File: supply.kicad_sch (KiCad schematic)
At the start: 151 parts, among them IC1 TPS54561, J3 DC_SOCKET, J8 61300311121, U10 LM3881MME_NOPB, U12 AP62301WU-7, U17 SN74LVC1G125DBVR, U18 MAX812REUS+T, U19 PAC1954T-E/4MX, U2 TPS65295RJET, U20 PAC1954T-E/4MX, U21 SN74LVC1G125DBVR, U22 SN74LVC1G125DBVR, U23 SN74LVC1G125DBVR, U4 AP62301WU-7, U5 AP62301WU-7, U9 AP62301WU-7

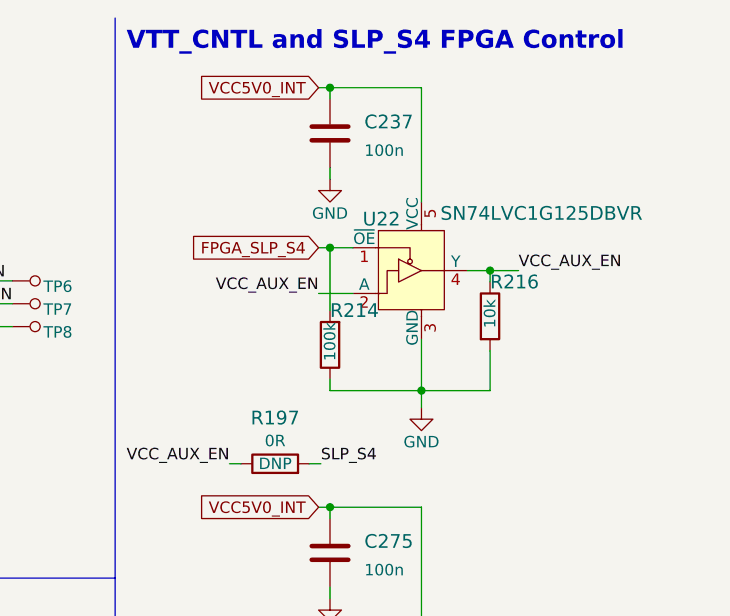
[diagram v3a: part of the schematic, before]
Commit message: All components inside the board area, fix FMC column B shift on schematic, add PCIe layer dependent rules
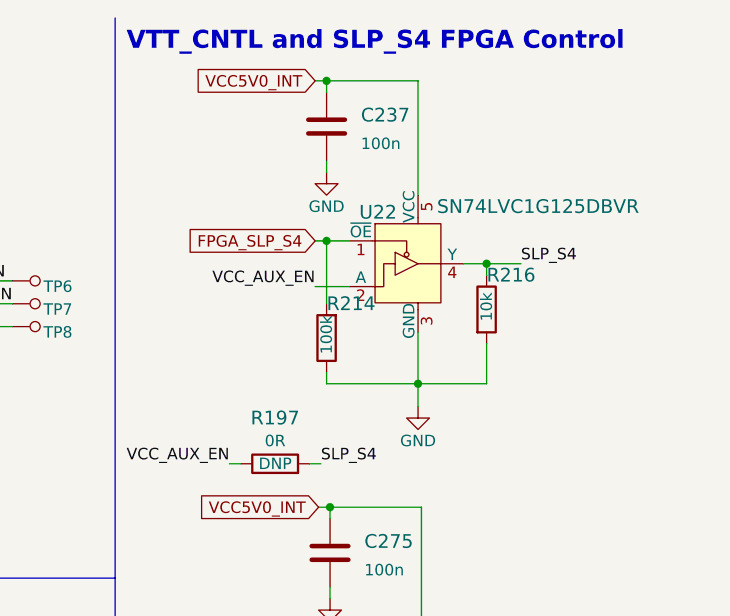
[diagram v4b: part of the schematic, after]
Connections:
- net SLP_S4: now also R216.1, U22.4 (Y)
- net VCC_AUX_EN: no longer R216.1, U22.4 (Y)
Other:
- moved on the sheet: C237, R214, R216, U22

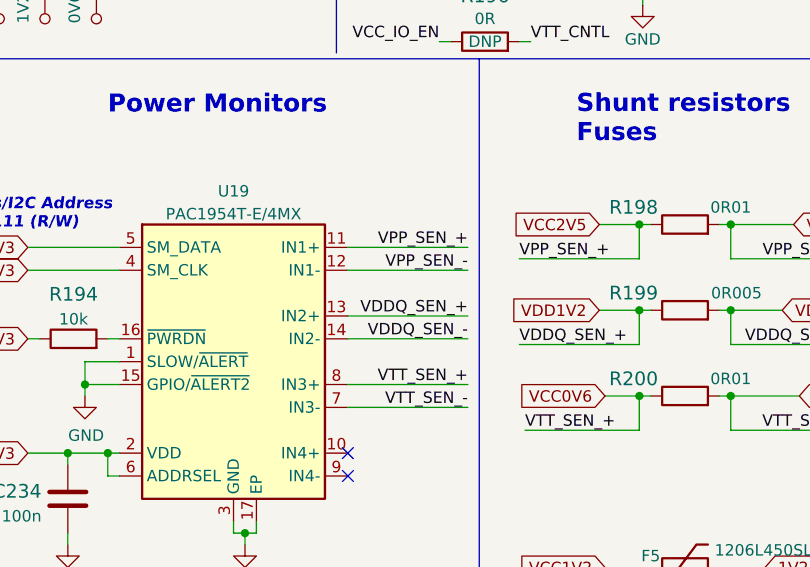
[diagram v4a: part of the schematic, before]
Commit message: Add ETH MUX passthrough, reroute HDMI to 100 Ohm differential, begin routing current measurment circuit
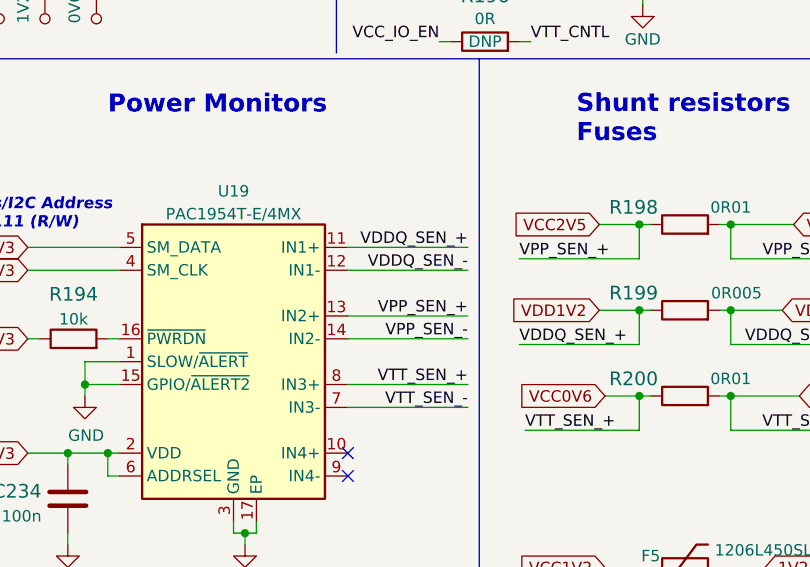
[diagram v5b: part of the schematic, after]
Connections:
- net VCC2V5: now also U19.13 (IN2+); no longer U19.11 (IN1+)
- net VDD1V2: now also U19.11 (IN1+); no longer U19.13 (IN2+)
- net VDDQ: now also U19.12 (IN1-); no longer U19.14 (IN2-)
- net VPP: now also U19.14 (IN2-); no longer U19.12 (IN1-)
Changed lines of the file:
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@@
     (stroke (width 0) (type default) (color 0 0 0 0))
   )
-  (wire (pts (xy 346.71 139.7) (xy 360.045 139.7))
+  (wire (pts (xy 346.71 132.08) (xy 360.045 132.08))
     (stroke (width 0) (type default) (color 0 0 0 0))
   )
@@
     (stroke (width 0) (type default) (color 0 0 0 0))
   )
-  (wire (pts (xy 346.71 132.08) (xy 360.045 132.08))
+  (wire (pts (xy 346.71 139.7) (xy 360.045 139.7))
     (stroke (width 0) (type default) (color 0 0 0 0))
   )
@@
     (stroke (width 0) (type default) (color 0 0 0 0))
   )
-  (wire (pts (xy 346.71 137.16) (xy 360.045 137.16))
+  (wire (pts (xy 346.71 129.54) (xy 360.045 129.54))
     (stroke (width 0) (type default) (color 0 0 0 0))
   )
@@
     (stroke (width 0) (type default) (color 0 0 0 0))
   )
-  (wire (pts (xy 346.71 129.54) (xy 360.045 129.54))
+  (wire (pts (xy 346.71 137.16) (xy 360.045 137.16))
     (stroke (width 0) (type default) (color 0 0 0 0))
   )
@@
     (effects (font (size 1.27 1.27)) (justify right bottom))
   )
-  (label "VDDQ_SEN_+" (at 360.045 137.16 180)
+  (label "VDDQ_SEN_+" (at 360.045 129.54 180)
     (effects (font (size 1.27 1.27)) (justify right bottom))
   )
@@
     (effects (font (size 1.27 1.27)) (justify right bottom))
   )
-  (label "VPP_SEN_+" (at 360.045 129.54 180)
+  (label "VPP_SEN_+" (at 360.045 137.16 180)
     (effects (font (size 1.27 1.27)) (justify right bottom))
   )
@@
     (effects (font (size 1.27 1.27)) (justify left bottom))
   )
-  (label "VDDQ_SEN_-" (at 360.045 139.7 180)
+  (label "VDDQ_SEN_-" (at 360.045 132.08 180)
     (effects (font (size 1.27 1.27)) (justify right bottom))
   )
@@
     (effects (font (size 1.27 1.27)) (justify left bottom))
   )
-  (label "VPP_SEN_-" (at 360.045 132.08 180)
+  (label "VPP_SEN_-" (at 360.045 139.7 180)
     (effects (font (size 1.27 1.27)) (justify right bottom))
   )

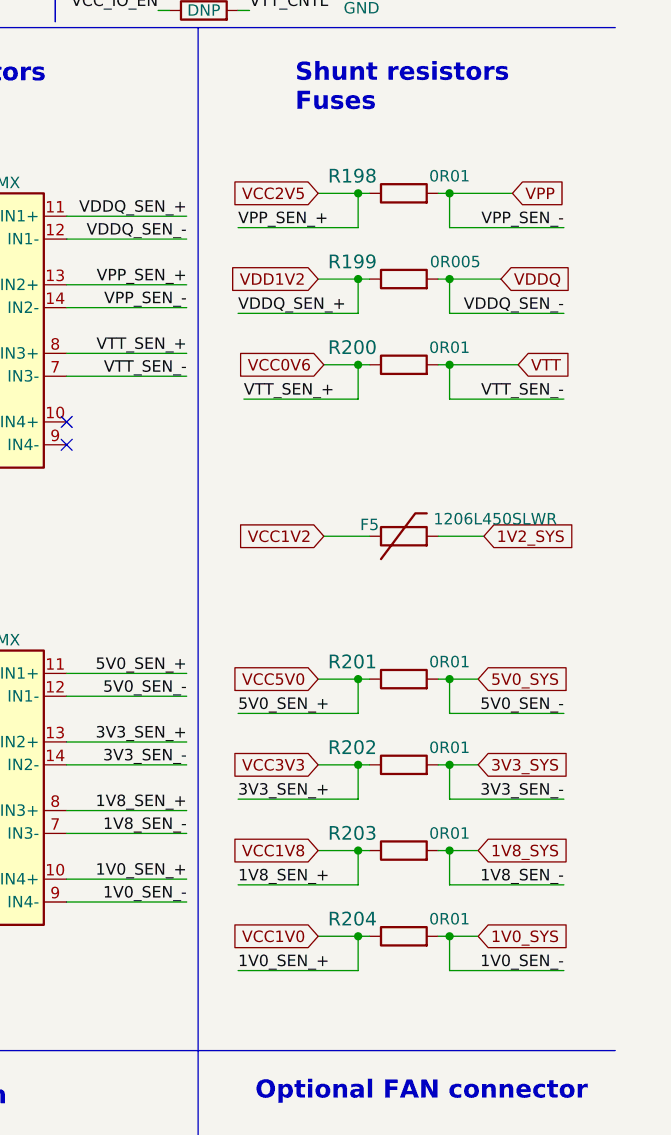
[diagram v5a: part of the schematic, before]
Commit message: Add kelvin connection to shunt resistors, move some data, control and address traces from layer In.9 to In.5, route current measurment circuit
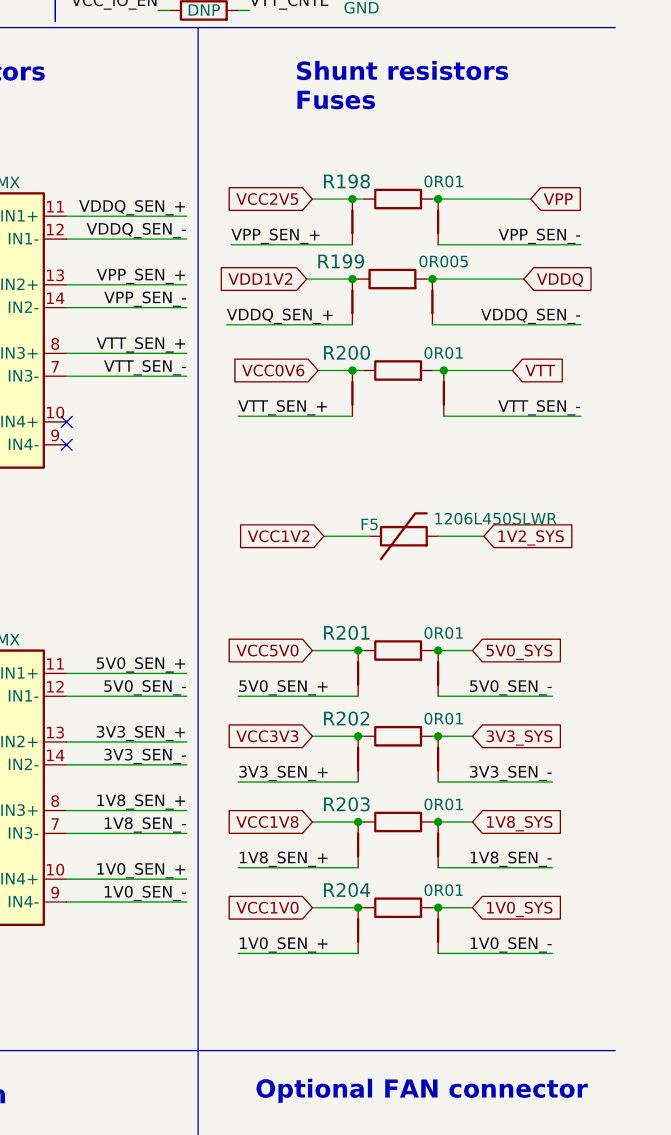
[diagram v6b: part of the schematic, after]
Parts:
- added NT1, NT10, NT11, NT12, NT13, NT14, NT2, NT3, NT4, NT5, NT6, NT7, NT8, NT9: NetTie_2, antmicro-footprints:NetTie-2_SMD_Pad0.127mm, symbol antmicroShuntsJumpers:NetTie_2
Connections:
- net 1V0_SYS: now also NT14.2; no longer U20.9 (IN4-)
- net 1V8_SYS: now also NT13.2; no longer U20.7 (IN3-)
- net 3V3_SYS: now also NT12.2; no longer U20.14 (IN2-)
- net 5V0_SYS: now also NT11.2; no longer U20.12 (IN1-)
- net VCC0V6: now also NT3.2; no longer U19.8 (IN3+)
- net VCC1V0: now also NT10.2; no longer U20.10 (IN4+)
- net VCC1V8: now also NT9.2; no longer U20.8 (IN3+)
- net VCC2V5: now also NT1.2; no longer U19.13 (IN2+)
- net VCC3V3: now also NT8.2; no longer U20.13 (IN2+)
- net VCC5V0: now also NT7.2; no longer U20.11 (IN1+)
- net VDD1V2: now also NT2.2; no longer U19.11 (IN1+)
- net VDDQ: now also NT4.2; no longer U19.12 (IN1-)
- net VPP: now also NT5.2; no longer U19.14 (IN2-)
- net VTT: now also NT6.2; no longer U19.7 (IN3-)
- new net 1V0_SEN_+: NT10.1, U20.10 (IN4+)
- new net 1V0_SEN_-: NT14.1, U20.9 (IN4-)
- new net 1V8_SEN_+: NT9.1, U20.8 (IN3+)
- new net 1V8_SEN_-: NT13.1, U20.7 (IN3-)
- new net 3V3_SEN_+: NT8.1, U20.13 (IN2+)
- new net 3V3_SEN_-: NT12.1, U20.14 (IN2-)
- new net 5V0_SEN_+: NT7.1, U20.11 (IN1+)
- new net 5V0_SEN_-: NT11.1, U20.12 (IN1-)
- new net VDDQ_SEN_+: NT2.1, U19.11 (IN1+)
- new net VDDQ_SEN_-: NT4.1, U19.12 (IN1-)
- new net VPP_SEN_+: NT1.1, U19.13 (IN2+)
- new net VPP_SEN_-: NT5.1, U19.14 (IN2-)
- new net VTT_SEN_+: NT3.1, U19.8 (IN3+)
- new net VTT_SEN_-: NT6.1, U19.7 (IN3-)
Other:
- moved on the sheet: R198, R199, R200, R201, R202, R203, R204

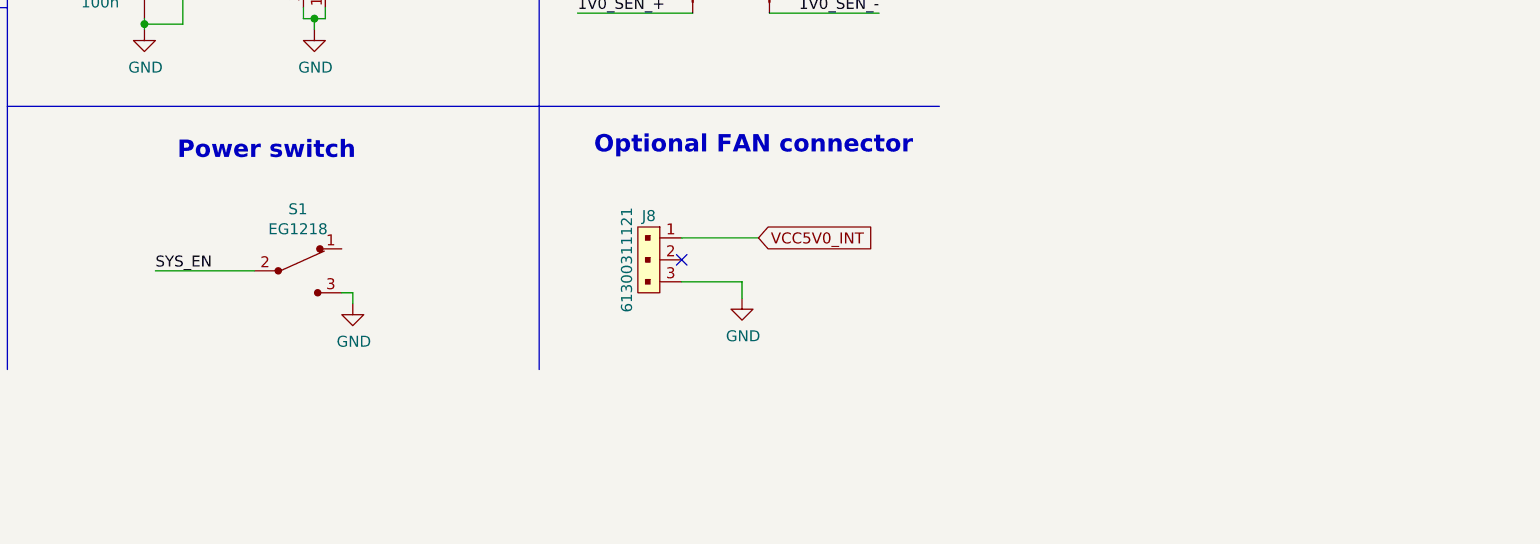
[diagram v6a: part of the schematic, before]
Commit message: Implement LED and PB mechanical concept. Assign bank 15 to FMC, remove buttons and add new ones
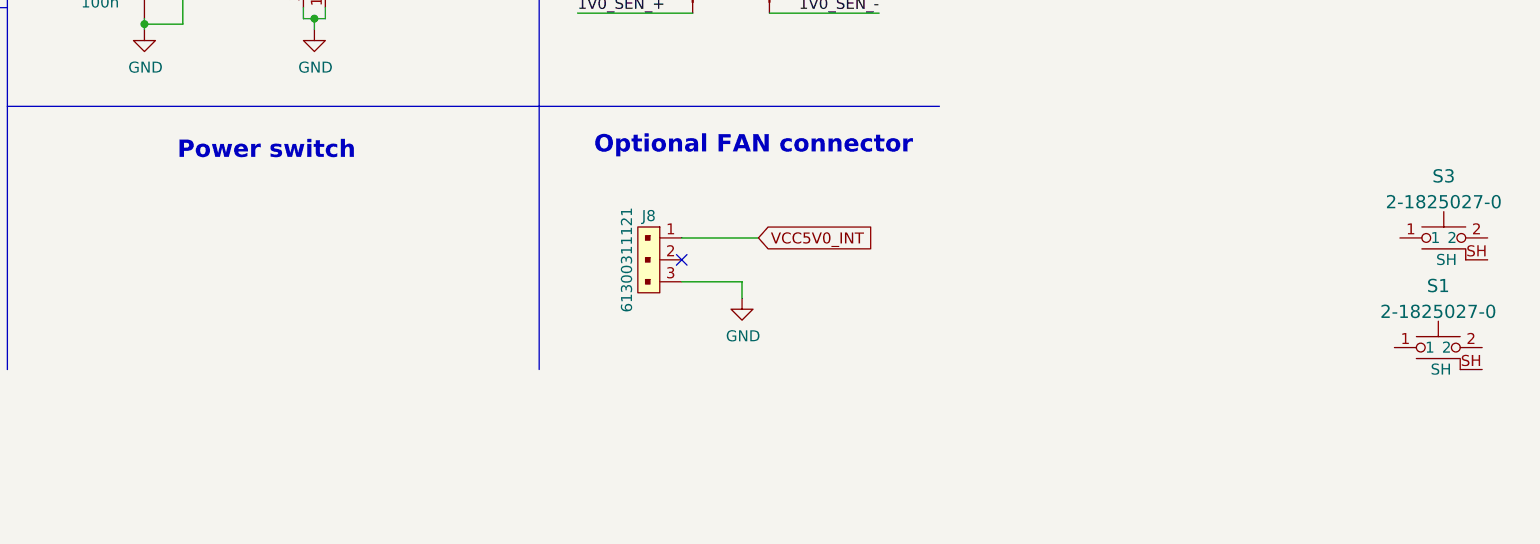
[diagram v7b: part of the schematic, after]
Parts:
- removed S1: EG1218, data-center-dram-tester-footprints:Switch_Slide_11.6x4mm_EG1218, symbol data-center-dram-tester:EG1218
- added S1, S3: 2-1825027-0, antmicro-footprints:TE_2-1825027-0, symbol antmicroTactileSwitches:2-1825027-0
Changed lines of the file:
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@@
     (stroke (width 0) (type default) (color 0 0 0 0))
   )
-  (wire (pts (xy 339.725 243.84) (xy 339.725 245.11))
-    (stroke (width 0) (type default) (color 0 0 0 0))
-  )
   (wire (pts (xy 287.02 41.91) (xy 275.59 41.91))
     (stroke (width 0) (type default) (color 0 0 0 0))
@@
     (stroke (width 0) (type default) (color 0 0 0 0))
   )
-  (wire (pts (xy 328.295 241.3) (xy 316.865 241.3))
-    (stroke (width 0) (type default) (color 0 0 0 0))
-  )
   (wire (pts (xy 185.42 234.95) (xy 188.595 234.95))
     (stroke (width 0) (type default) (color 0 0 0 0))
@@
     (stroke (width 0) (type default) (color 0 0 0 0))
   )
-  (wire (pts (xy 338.455 243.84) (xy 339.725 243.84))
-    (stroke (width 0) (type default) (color 0 0 0 0))
-  )
   (wire (pts (xy 217.932 99.06) (xy 217.932 100.965))
     (stroke (width 0) (type default) (color 0 0 0 0))
@@
     (effects (font (size 1.27 1.27)) (justify right bottom))
   )
-  (label "SYS_EN" (at 316.865 241.3 0)
-    (effects (font (size 1.27 1.27)) (justify left bottom))
-  )
   (label "SYS_PWR_GOOD" (at 123.825 151.13 180)
     (effects (font (size 1.27 1.27)) (justify right bottom))
@@
     (pin "1")
   )
-  (symbol (lib_id "data-center-dram-tester:GND") (at 339.725 245.11 0) (unit 1)
-    (in_bom yes) (on_board yes)
-    (property "Reference" "#PWR035" (id 0) (at 339.725 251.46 0)
-      (effects (font (size 1.27 1.27)) hide)
-    )
-    (property "Value" "GND" (id 1) (at 339.852 249.5042 0))
-    (property "Footprint" "" (id 2) (at 339.725 245.11 0)
-      (effects (font (size 1.27 1.27)) hide)
-    )
-    (property "Datasheet" "" (id 3) (at 339.725 245.11 0)
-      (effects (font (size 1.27 1.27)) hide)
-    )
-    (pin "1")
-  )
   (symbol (lib_id "data-center-dram-tester:TP_SMD1MM") (at 307.975 104.14 0) (unit 1)
     (in_bom yes) (on_board yes)
@@
     (pin "1")
   )
-  (symbol (lib_id "data-center-dram-tester:EG1218") (at 333.375 241.3 0) (unit 1)
-    (in_bom yes) (on_board yes)
-    (property "Reference" "S1" (id 0) (at 333.375 234.1626 0))
-    (property "Value" "EG1218" (id 1) (at 333.375 236.474 0))
-    (property "Footprint" "data-center-dram-tester-footprints:Switch_Slide_11.6x4mm_EG1218" (id 2) (at 338.455 236.22 0)
-      (effects (font (size 1.27 1.27)) (justify left) hide)
-    )
-    (property "Datasheet" "http://spec_sheets.e-switch.com/specs/P040040.pdf" (id 3) (at 338.455 233.68 0)
-      (effects (font (size 1.524 1.524)) (justify left) hide)
-    )
-    (property "MPN" "EG1218" (id 4) (at 338.455 228.6 0)
-      (effects (font (size 1.524 1.524)) (justify left) hide)
-    )
-    (property "Manufacturer" "E-Switch" (id 5) (at 338.455 213.36 0)
-      (effects (font (size 1.524 1.524)) (justify left) hide)
-    )
-    (pin "1")
-    (pin "2")
-    (pin "3")
-  )
   (symbol (lib_id "data-center-dram-tester:61300311121") (at 374.015 237.49 270) (unit 1)
     (in_bom yes) (on_board yes)
@@
     (pin "2")
   )
+  (symbol (lib_id "antmicroTactileSwitches:2-1825027-0") (at 465.455 248.92 0) (unit 1)
+    (in_bom yes) (on_board yes) (fields_autoplaced)
+    (property "Reference" "S1" (id 0) (at 465.455 243.0579 0)
+      (effects (font (size 1.524 1.524)))
+    )
+    (property "Value" "2-1825027-0" (id 1) (at 465.455 246.0513 0)
+      (effects (font (size 1.524 1.524)))
+    )
+    (property "Footprint" "antmicro-footprints:TE_2-1825027-0" (id 2) (at 470.535 243.84 0)
+      (effects (font (size 1.524 1.524)) (justify left) hide)
+    )
+    (property "Datasheet" "https://www.te.com/commerce/DocumentDelivery/DDEController?Action=showdoc&DocId=Customer+Drawing%7F1825027%7FH1%7Fpdf%7FEnglish%7FENG_CD_1825027_H1.pdf%7F2-1825027-0" (id 3) (at 470.535 241.3 0)
+      (effects (font (size 1.524 1.524)) (justify left) hide)
+    )
+    (property "MPN" "2-1825027-0" (id 4) (at 470.535 236.22 0)
+      (effects (font (size 1.524 1.524)) (justify left) hide)
+    )
+    (property "Manufacturer" "TE Connectivity" (id 5) (at 470.535 220.98 0)
+      (effects (font (size 1.524 1.524)) (justify left) hide)
+    )
+    (pin "1")
+    (pin "2")
+    (pin "SH")
+  )
   (symbol (lib_id "antmicroPMICPowerSequencers:MAX812REUS+T") (at 232.41 35.56 0) (unit 1)
     (in_bom yes) (on_board yes) (fields_autoplaced)
@@
     (pin "4")
   )
+  (symbol (lib_id "antmicroTactileSwitches:2-1825027-0") (at 466.09 236.22 0) (unit 1)
+    (in_bom yes) (on_board yes) (fields_autoplaced)
+    (property "Reference" "S3" (id 0) (at 466.09 230.3579 0)
+      (effects (font (size 1.524 1.524)))
+    )
+    (property "Value" "2-1825027-0" (id 1) (at 466.09 233.3513 0)
+      (effects (font (size 1.524 1.524)))
+    )
+    (property "Footprint" "antmicro-footprints:TE_2-1825027-0" (id 2) (at 471.17 231.14 0)
+      (effects (font (size 1.524 1.524)) (justify left) hide)
+    )
+    (property "Datasheet" "https://www.te.com/commerce/DocumentDelivery/DDEController?Action=showdoc&DocId=Customer+Drawing%7F1825027%7FH1%7Fpdf%7FEnglish%7FENG_CD_1825027_H1.pdf%7F2-1825027-0" (id 3) (at 471.17 228.6 0)
+      (effects (font (size 1.524 1.524)) (justify left) hide)
+    )
+    (property "MPN" "2-1825027-0" (id 4) (at 471.17 223.52 0)
+      (effects (font (size 1.524 1.524)) (justify left) hide)
+    )
+    (property "Manufacturer" "TE Connectivity" (id 5) (at 471.17 208.28 0)
+      (effects (font (size 1.524 1.524)) (justify left) hide)
+    )
+    (pin "1")
+    (pin "2")
+    (pin "SH")
+  )
   (symbol (lib_id "antmicroResistorsmisc:R_0R005_1206") (at 382.905 136.525 0) (unit 1)
